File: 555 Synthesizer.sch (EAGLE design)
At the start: 40 parts, among them IC1 555, Q1 FQP27P06, U1 LM7805

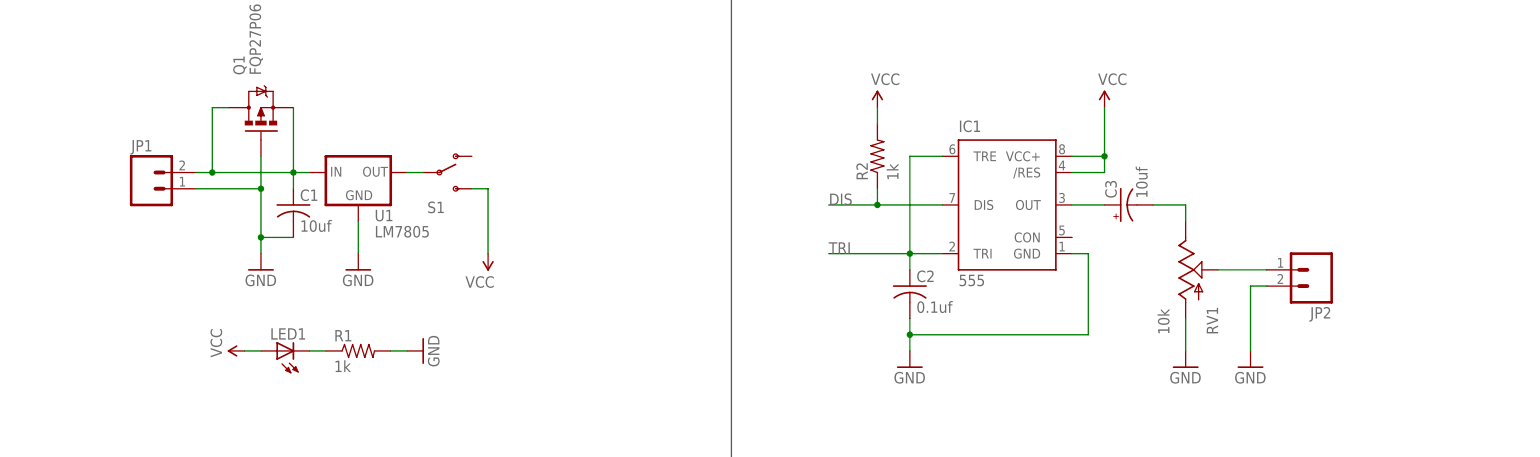
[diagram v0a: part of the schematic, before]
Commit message: Added CMOS 555
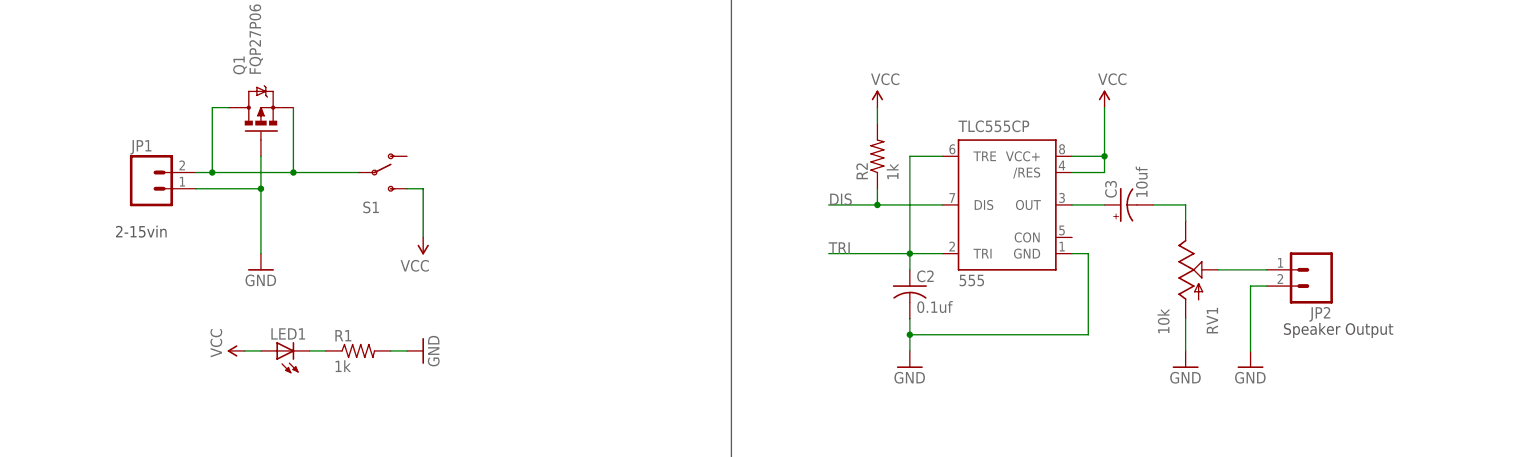
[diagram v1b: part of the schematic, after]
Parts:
- removed C1: 10uf, adafruit:C-US025-030X050
- removed U1: LM7805, SparkFun-PowerIC:V_REG_78XXSINK
- renumbered IC1 to TLC555CP
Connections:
- removed net N$3: S1.P, U1.OUT
- net GND: no longer C1.2, U1.GND
- net N$1: now also S1.P; no longer C1.1, U1.IN
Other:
- note added: "2-15vin"
- note added: "Speaker Output"
- moved on the sheet: S1
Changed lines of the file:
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@@
 <?xml version="1.0" encoding="utf-8"?>
 <!DOCTYPE eagle SYSTEM "eagle.dtd">
-<eagle version="7.3.0">
+<eagle version="7.4.0">
 <drawing>
 <settings>
@@
 <part name="S1" library="SparkFun-Electromechanical" deviceset="SWITCH-SPDT" device="KIT"/>
 <part name="LED1" library="adafruit" deviceset="LED" device="5MM"/>
-<part name="GND3" library="SparkFun-Aesthetics" deviceset="GND" device=""/>
 <part name="SUPPLY1" library="SparkFun-Aesthetics" deviceset="VCC" device=""/>
 <part name="SUPPLY2" library="SparkFun-Aesthetics" deviceset="VCC" device=""/>
 <part name="GND4" library="SparkFun-Aesthetics" deviceset="GND" device=""/>
-<part name="IC1" library="SparkFun-AnalogIC" deviceset="NE555" device="KIT" value="555"/>
+<part name="TLC555CP" library="SparkFun-AnalogIC" deviceset="NE555" device="KIT" value="555"/>
 <part name="SUPPLY3" library="SparkFun-Aesthetics" deviceset="VCC" device=""/>
 <part name="SUPPLY4" library="SparkFun-Aesthetics" deviceset="VCC" device=""/>
@@
 <part name="S2" library="SparkFun-Retired" deviceset="TAC_SWITCH" device="PTH"/>
 <part name="JP2" library="SparkFun-Connectors" deviceset="M02" device="3.5MM"/>
-<part name="U1" library="SparkFun-PowerIC" deviceset="V_REG_78XX" device="SINK" value="LM7805"/>
 <part name="Q1" library="SparkFun-DiscreteSemi" deviceset="MOSFET-PCHANNEL" device="FQP27P06" value="FQP27P06"/>
 <part name="R3" library="adafruit" deviceset="R-US_" device="0204/7" value="1k"/>
@@
 <part name="R1" library="adafruit" deviceset="R-US_" device="0204/7" value="1k"/>
 <part name="C3" library="adafruit" deviceset="CPOL-US" device="E2,5-6E" value="10uf"/>
-<part name="C1" library="adafruit" deviceset="C-US" device="025-030X050" value="10uf"/>
 <part name="C2" library="adafruit" deviceset="C-US" device="025-025X050" value="0.1uf"/>
 <part name="FRAME1" library="SparkFun-Aesthetics" deviceset="FRAME-LETTER" device="NO_PACKAGE"/>
@@
 <wire x1="119.38" y1="88.9" x2="119.38" y2="185.42" width="0.1524" layer="97"/>
 <text x="243.84" y="7.62" size="3.81" layer="97" font="vector">2</text>
+<text x="22.86" y="142.24" size="1.778" layer="97">2-15vin</text>
+<text x="205.74" y="127" size="1.778" layer="97">Speaker Output</text>
 </plain>
 <instances>
 <instance part="GND2" gate="1" x="45.72" y="137.16"/>
 <instance part="JP1" gate="G$1" x="27.94" y="149.86"/>
-<instance part="S1" gate="1" x="73.66" y="152.4"/>
+<instance part="S1" gate="1" x="63.5" y="152.4"/>
 <instance part="LED1" gate="G$1" x="48.26" y="124.46" rot="R90"/>
-<instance part="GND3" gate="1" x="60.96" y="137.16"/>
-<instance part="SUPPLY1" gate="G$1" x="81.28" y="139.7" rot="R180"/>
+<instance part="SUPPLY1" gate="G$1" x="71.12" y="142.24" rot="R180"/>
 <instance part="SUPPLY2" gate="G$1" x="43.18" y="124.46" rot="R90"/>
 <instance part="GND4" gate="1" x="71.12" y="124.46" rot="R90"/>
-<instance part="IC1" gate="G$1" x="162.56" y="147.32"/>
+<instance part="TLC555CP" gate="G$1" x="162.56" y="147.32"/>
 <instance part="SUPPLY3" gate="G$1" x="177.8" y="162.56"/>
 <instance part="SUPPLY4" gate="G$1" x="142.24" y="162.56"/>
@@
 <instance part="S2" gate="S" x="22.86" y="53.34" rot="R90"/>
 <instance part="JP2" gate="G$1" x="210.82" y="137.16" rot="R180"/>
-<instance part="U1" gate="G$1" x="60.96" y="152.4"/>
 <instance part="Q1" gate="G$1" x="45.72" y="162.56" rot="R90"/>
 <instance part="R3" gate="G$1" x="30.48" y="58.42"/>
@@
 <instance part="R1" gate="G$1" x="60.96" y="124.46"/>
 <instance part="C3" gate="G$1" x="180.34" y="147.32" rot="R90"/>
-<instance part="C1" gate="G$1" x="50.8" y="147.32"/>
 <instance part="C2" gate="G$1" x="147.32" y="134.62"/>
 <instance part="FRAME1" gate="G$1" x="0" y="0"/>
@@
 <segment>
 <pinref part="GND2" gate="1" pin="GND"/>
-<wire x1="45.72" y1="139.7" x2="45.72" y2="142.24" width="0.1524" layer="91"/>
 <pinref part="JP1" gate="G$1" pin="1"/>
-<wire x1="45.72" y1="142.24" x2="45.72" y2="149.86" width="0.1524" layer="91"/>
+<wire x1="45.72" y1="139.7" x2="45.72" y2="149.86" width="0.1524" layer="91"/>
 <wire x1="45.72" y1="149.86" x2="35.56" y2="149.86" width="0.1524" layer="91"/>
-<wire x1="50.8" y1="142.24" x2="45.72" y2="142.24" width="0.1524" layer="91"/>
-<junction x="45.72" y="142.24"/>
 <pinref part="Q1" gate="G$1" pin="G"/>
 <wire x1="45.72" y1="154.94" x2="45.72" y2="149.86" width="0.1524" layer="91"/>
 <junction x="45.72" y="149.86"/>
-<pinref part="C1" gate="G$1" pin="2"/>
-</segment>
-<segment>
-<pinref part="GND3" gate="1" pin="GND"/>
-<wire x1="60.96" y1="139.7" x2="60.96" y2="144.78" width="0.1524" layer="91"/>
-<pinref part="U1" gate="G$1" pin="GND"/>
 </segment>
 <segment>
@@
 <pinref part="GND1" gate="1" pin="GND"/>
 <wire x1="147.32" y1="124.46" x2="147.32" y2="127" width="0.1524" layer="91"/>
-<pinref part="IC1" gate="G$1" pin="GND"/>
+<pinref part="TLC555CP" gate="G$1" pin="GND"/>
 <wire x1="147.32" y1="127" x2="147.32" y2="129.54" width="0.1524" layer="91"/>
 <wire x1="172.72" y1="139.7" x2="175.26" y2="139.7" width="0.1524" layer="91"/>
@@
 </segment>
 </net>
-<net name="N$3" class="0">
-<segment>
-<pinref part="S1" gate="1" pin="P"/>
-<wire x1="68.58" y1="152.4" x2="71.12" y2="152.4" width="0.1524" layer="91"/>
-<pinref part="U1" gate="G$1" pin="OUT"/>
-</segment>
-</net>
 <net name="VCC" class="0">
 <segment>
@@
 <pinref part="SUPPLY1" gate="G$1" pin="VCC"/>
 <pinref part="S1" gate="1" pin="S"/>
-<wire x1="78.74" y1="149.86" x2="81.28" y2="149.86" width="0.1524" layer="91"/>
-<wire x1="81.28" y1="139.7" x2="81.28" y2="149.86" width="0.1524" layer="91"/>
-</segment>
-<segment>
-<pinref part="IC1" gate="G$1" pin="VCC+"/>
+<wire x1="68.58" y1="149.86" x2="71.12" y2="149.86" width="0.1524" layer="91"/>
+<wire x1="71.12" y1="142.24" x2="71.12" y2="149.86" width="0.1524" layer="91"/>
+</segment>
+<segment>
+<pinref part="TLC555CP" gate="G$1" pin="VCC+"/>
 <wire x1="172.72" y1="154.94" x2="177.8" y2="154.94" width="0.1524" layer="91"/>
 <wire x1="177.8" y1="154.94" x2="177.8" y2="152.4" width="0.1524" layer="91"/>
-<pinref part="IC1" gate="G$1" pin="/RES"/>
+<pinref part="TLC555CP" gate="G$1" pin="/RES"/>
 <wire x1="177.8" y1="152.4" x2="172.72" y2="152.4" width="0.1524" layer="91"/>
 <wire x1="177.8" y1="154.94" x2="177.8" y2="162.56" width="0.1524" layer="91"/>
@@
 <net name="DIS" class="0">
 <segment>
-<pinref part="IC1" gate="G$1" pin="DIS"/>
+<pinref part="TLC555CP" gate="G$1" pin="DIS"/>
 <wire x1="152.4" y1="147.32" x2="142.24" y2="147.32" width="0.1524" layer="91"/>
 <wire x1="142.24" y1="147.32" x2="142.24" y2="149.86" width="0.1524" layer="91"/>
@@
 <net name="TRI" class="0">
 <segment>
-<pinref part="IC1" gate="G$1" pin="TRI"/>
+<pinref part="TLC555CP" gate="G$1" pin="TRI"/>
 <wire x1="152.4" y1="139.7" x2="147.32" y2="139.7" width="0.1524" layer="91"/>
 <wire x1="147.32" y1="139.7" x2="147.32" y2="137.16" width="0.1524" layer="91"/>
-<pinref part="IC1" gate="G$1" pin="TRE"/>
+<pinref part="TLC555CP" gate="G$1" pin="TRE"/>
 <wire x1="152.4" y1="154.94" x2="147.32" y2="154.94" width="0.1524" layer="91"/>
 <wire x1="147.32" y1="154.94" x2="147.32" y2="139.7" width="0.1524" layer="91"/>
@@
 <net name="N$6" class="0">
 <segment>
-<pinref part="IC1" gate="G$1" pin="OUT"/>
+<pinref part="TLC555CP" gate="G$1" pin="OUT"/>
 <wire x1="172.72" y1="147.32" x2="177.8" y2="147.32" width="0.1524" layer="91"/>
 <pinref part="C3" gate="G$1" pin="+"/>
@@
 <segment>
 <pinref part="JP1" gate="G$1" pin="2"/>
-<pinref part="U1" gate="G$1" pin="IN"/>
-<wire x1="50.8" y1="152.4" x2="53.34" y2="152.4" width="0.1524" layer="91"/>
-<wire x1="50.8" y1="152.4" x2="50.8" y2="149.86" width="0.1524" layer="91"/>
 <wire x1="35.56" y1="152.4" x2="38.1" y2="152.4" width="0.1524" layer="91"/>
 <junction x="50.8" y="152.4"/>
@@
 <pinref part="Q1" gate="G$1" pin="S"/>
 <wire x1="50.8" y1="162.56" x2="50.8" y2="152.4" width="0.1524" layer="91"/>
-<pinref part="C1" gate="G$1" pin="1"/>
-</segment>
-</net>
+<pinref part="S1" gate="1" pin="P"/>
+<wire x1="50.8" y1="152.4" x2="60.96" y2="152.4" width="0.1524" layer="91"/>
+</segment>
+</net>
